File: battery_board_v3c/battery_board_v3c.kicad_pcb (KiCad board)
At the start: 4 copper layers, 88 x 94.5 mm, 210 parts, among them IC2 PCT2075DP,118, IC3 RP2040_QFN56, IC4 LT3652IMSE#PBF, IC5 RV-3028-C7_32.768kHz_1ppm_TA_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, J1 Bypass, J10 Jetson, J11 BM04B-SRSS-TB(LF)(SN), J12 Z+_Cap_Connector, J14 Solar, J15 FC, J16 I2C Multiplexer Breakout, J17 ISS Foot, J18 Screw_Terminal_01x02, J19 BM04B-SRSS-TB(LF)(SN), J20 CAN1, J21 BM04B-SRSS-TB(LF)(SN), J22 CAN2, J23 Conn_ARM_JTAG_SWD_10, J24 USB_B_Micro, J25 Life Makes Lemonade, J26 BM04B-SRSS-TB(LF)(SN), J27 I2C0 Breakout, J3 Heater, J5 Foot0, J6 Foot1, J7 Foot2, J8 Foot3, J9 RBF, K1 APAN3105, Q1 IRF7458, Q10 IRLML2803, Q11 NDS8434, Q2 IRF7458, Q3 MBT2222ADW1T1, Q4 MMBT2222AT, Q5 MBT2222ADW1T1, Q6 IRLML2803, Q7 IRLML2803, Q8 NDS8434, Q9 NDS8434, SW1 KMR2, SW2 KMR2, U1 R5460N208AA, U11 MCP25625-E/ML, U12 INA219AxD, U13 MAX706RESA, U14 INA219AxD, U15 MAX31856, U2 1049, U3 TPS54226PWPRPWP14_2P31X2P46-L, U4 1049, U5 TPS54226PWPRPWP14_2P31X2P46-L, U6 TPS7A4501DCQT, U8 W25Q128JV, Y1 Crystal_GND24, Y2 Crystal_GND24

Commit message: Version 3c Hotfix
Mistakenly did not connect the SPI1_CS1 pin to the breakout. Fixed in this new version.
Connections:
- J21 pad 1: SPI1_CS0 -> SPI1_CS1
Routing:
- net SPI1_CS1: track 0.00 -> 9.41 mm
- net +3V3: track 96.4 -> 103.2 mm, vias 41 -> 42
- net CAN_INT: track 31.4 -> 26.6 mm
- net SPI1_CS0: track 67.1 -> 65.4 mm, vias 6 -> 4
- net RTC_INT: track 49.5 -> 50.2 mm
- net D+: track 95.2 -> 94.7 mm
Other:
- board text removed: "Lay the relay!"

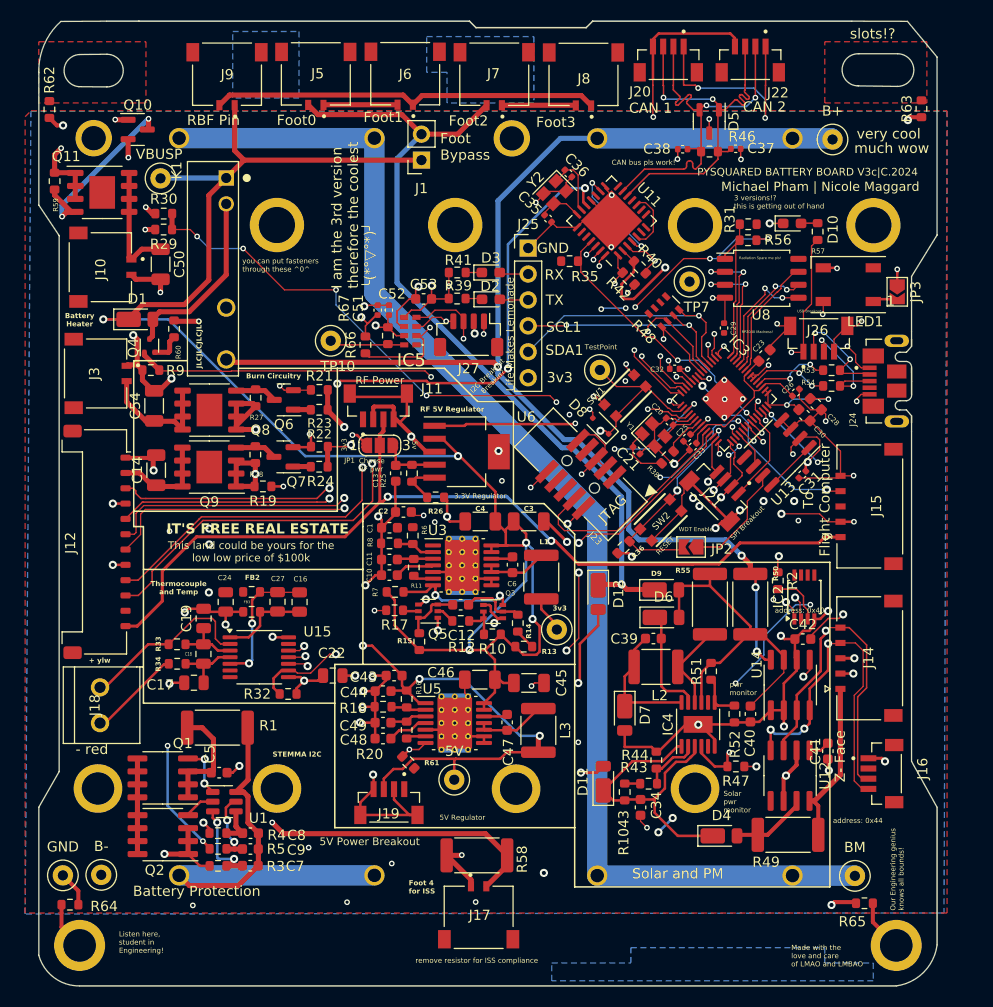
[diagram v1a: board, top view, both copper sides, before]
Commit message: V3c HOTFIX
Changes:
- Fixed swapped pins on the thermocouple SPI Lines
- Changed the 5V output to match requirements for the WatchDog Bias Circuit
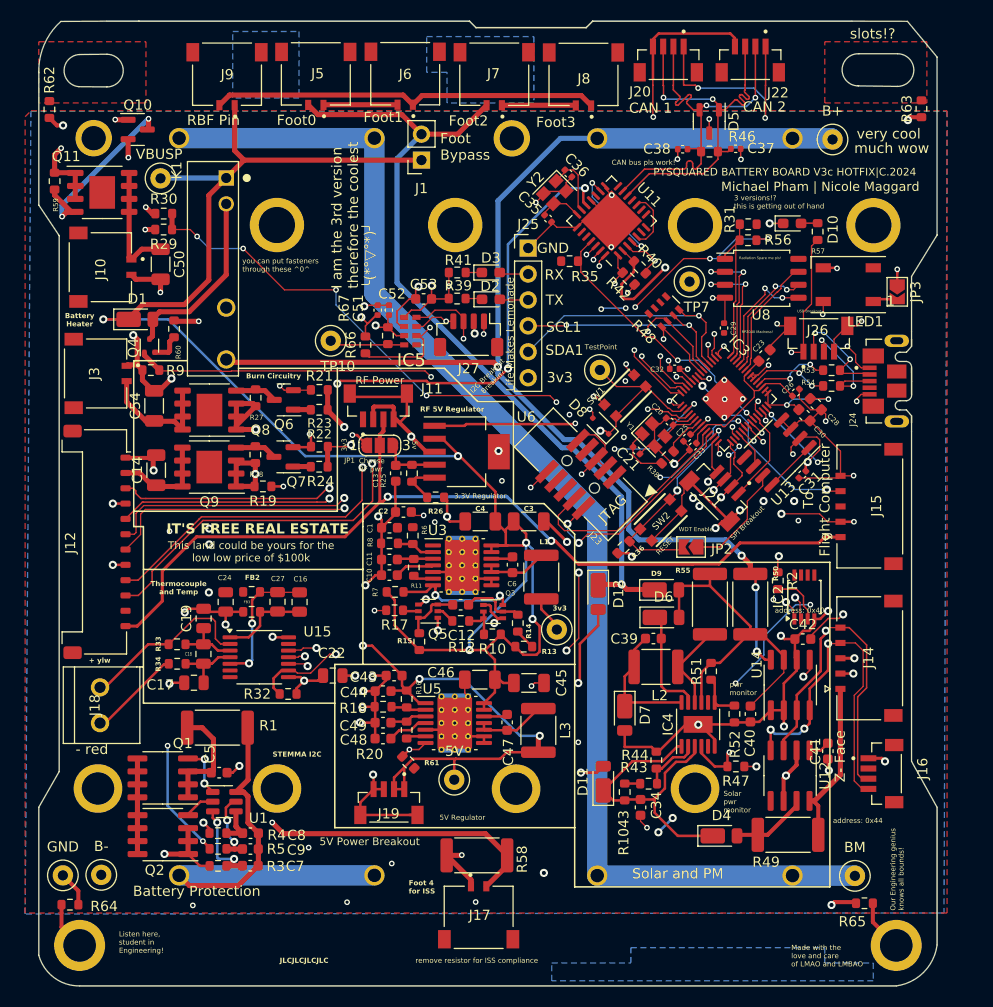
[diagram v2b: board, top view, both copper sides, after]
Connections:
- J19 pad 1: +3V3 -> +5V
- J19 pad 2: GND -> +5V
- J19 pad 3: +5V -> GND
- U15 pad 11: SPI1_MOSI -> SPI1_MISO
- U15 pad 12: SPI1_MISO -> SPI1_MOSI
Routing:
- net +5V: track 117.0 -> 119.1 mm
- net GND: track 326.5 -> 324.3 mm
- net SPI1_MISO: track 58.1 -> 59.0 mm
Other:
- board text added: "PYSQUARED BATTERY BOARD V3c HOTFIX|C.2024"
- board text removed: "PYSQUARED BATTERY BOARD V3c|C.2024"
